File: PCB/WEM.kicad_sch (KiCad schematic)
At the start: 0 parts

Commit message: Started schematic design
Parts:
- added D1: SMF5V0A, Diode_SMD:D_SMF, symbol Diode:SMF5V0A
- added D2: TPD2EUSB30DRTR, TPD2EUSB30DRTR:SOTFL35P100X50-3N, symbol TPD2EUSB30DRTR:TPD2EUSB30DRTR
- added F1: 1206L110THYR, Fuse:Fuse_1206_3216Metric_Pad1.42x1.75mm_HandSolder, symbol 2026-01-18_16-05-31:1206L110THYR
- added J1: USB_C_Receptacle_USB2.0_14P, symbol Connector:USB_C_Receptacle_USB2.0_14P
- added R1, R2: 5.1K, Resistor_SMD:R_0805_2012Metric_Pad1.20x1.40mm_HandSolder, symbol Device:R
- added U1: nRF52840, Package_DFN_QFN:Nordic_AQFN-73-1EP_7x7mm_P0.5mm, symbol MCU_Nordic:nRF52840
- added U2: MCP73871-2CC, Package_DFN_QFN:QFN-20-1EP_4x4mm_P0.5mm_EP2.5x2.5mm, symbol Battery_Management:MCP73871-2CC
- added U3: ~, PAW3395DM-T6QU:DIP-16_PAW3395DM-T6QU, symbol PAW3395DM-T6QU:PAW3395DM-T6QU_C9900026834
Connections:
- new net: J1.A5 (CC1), R1.1
- new net: D1.1 (A1), F1.1
- new net: D1.2 (A2), J1.A4 (VBUS), J1.A9 (VBUS), J1.B4 (VBUS), J1.B9 (VBUS)
- new net: U2.1 (OUT), U2.20 (OUT)
- new net: U2.10 (V_{SS}), U2.11 (V_{SS}), U2.21 (V_{SS})
- new net: U2.14 (V_{BAT}), U2.15 (V_{BAT})
- new net: U2.18 (IN), U2.19 (IN)
- new net: J1.B5 (CC2), R2.1
- new net: U1.A22 (VDD), U1.AD14 (VDD), U1.AD23 (VDD), U1.B1 (VDD), U1.W1 (VDD)
- new net: U1.B7 (VSS), U1.EP (VSS)
- new net GND: D2.3 (GND), J1.A1 (GND), J1.A12 (GND), J1.B1 (GND), J1.B12 (GND), J1.S1 (SHIELD), R1.2, R2.2
- new net USB_D+: D2.1 (D+), J1.A6 (D+), J1.B6 (D+)
- new net USB_D-: D2.2 (D-), J1.A7 (D-), J1.B7 (D-)
- new net VBUS: F1.2
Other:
- note added: "USB-C port"
- title: (none) -> WEM (Wireless Extensible Mouse)

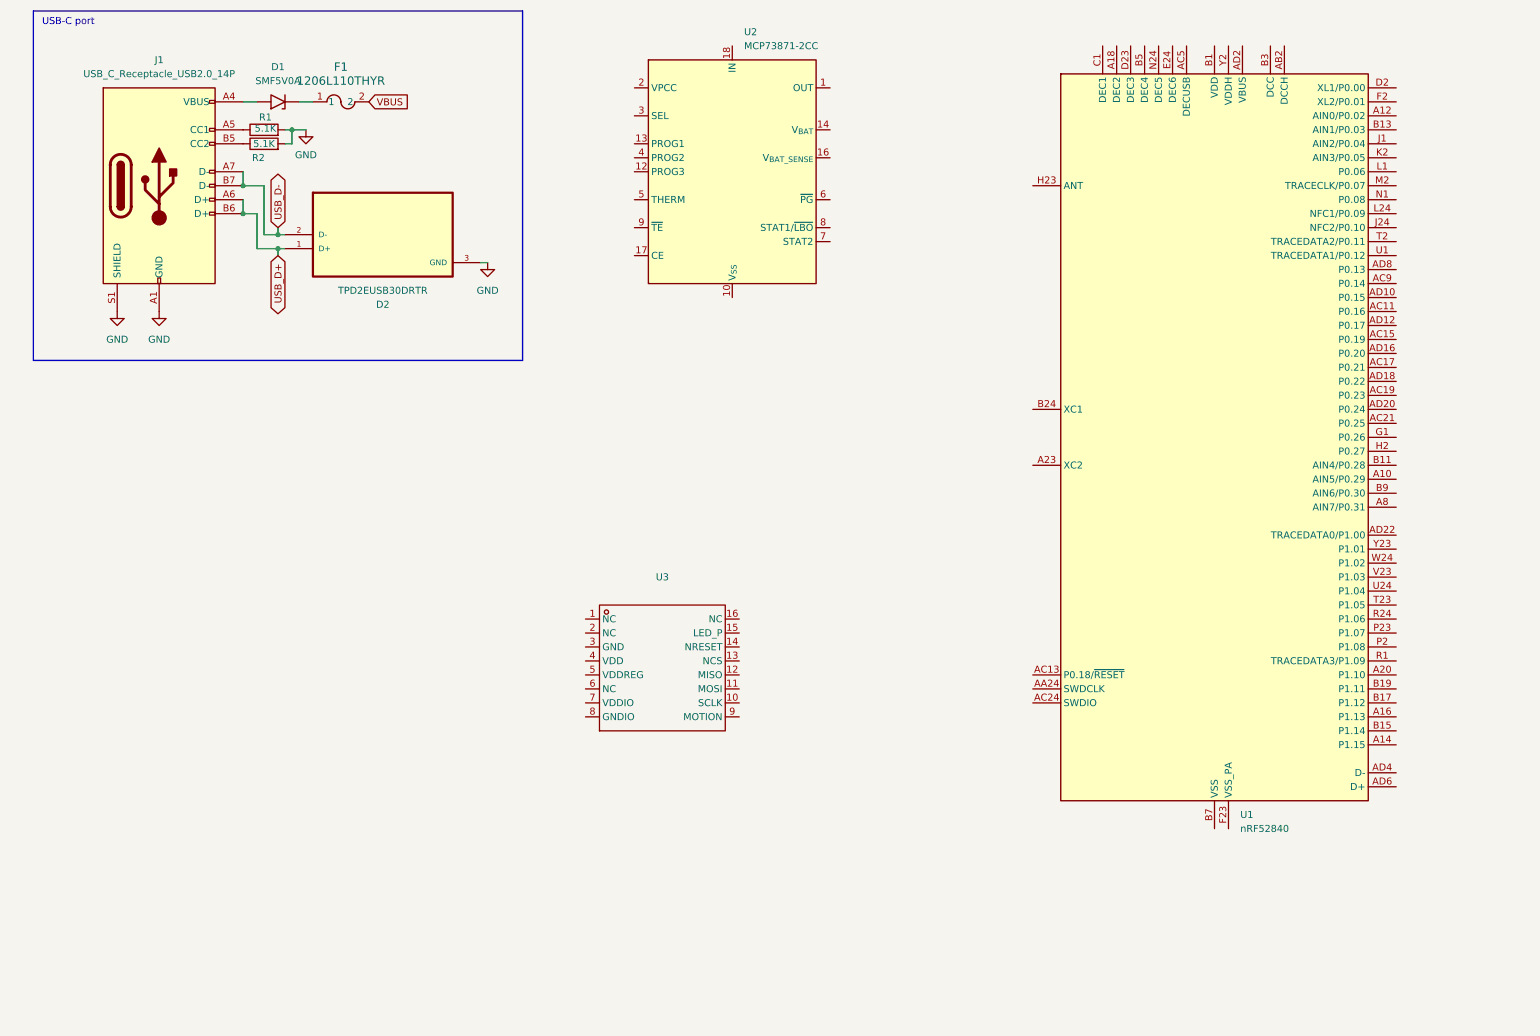
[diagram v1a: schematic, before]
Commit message: Voltage regulators and schematic progress
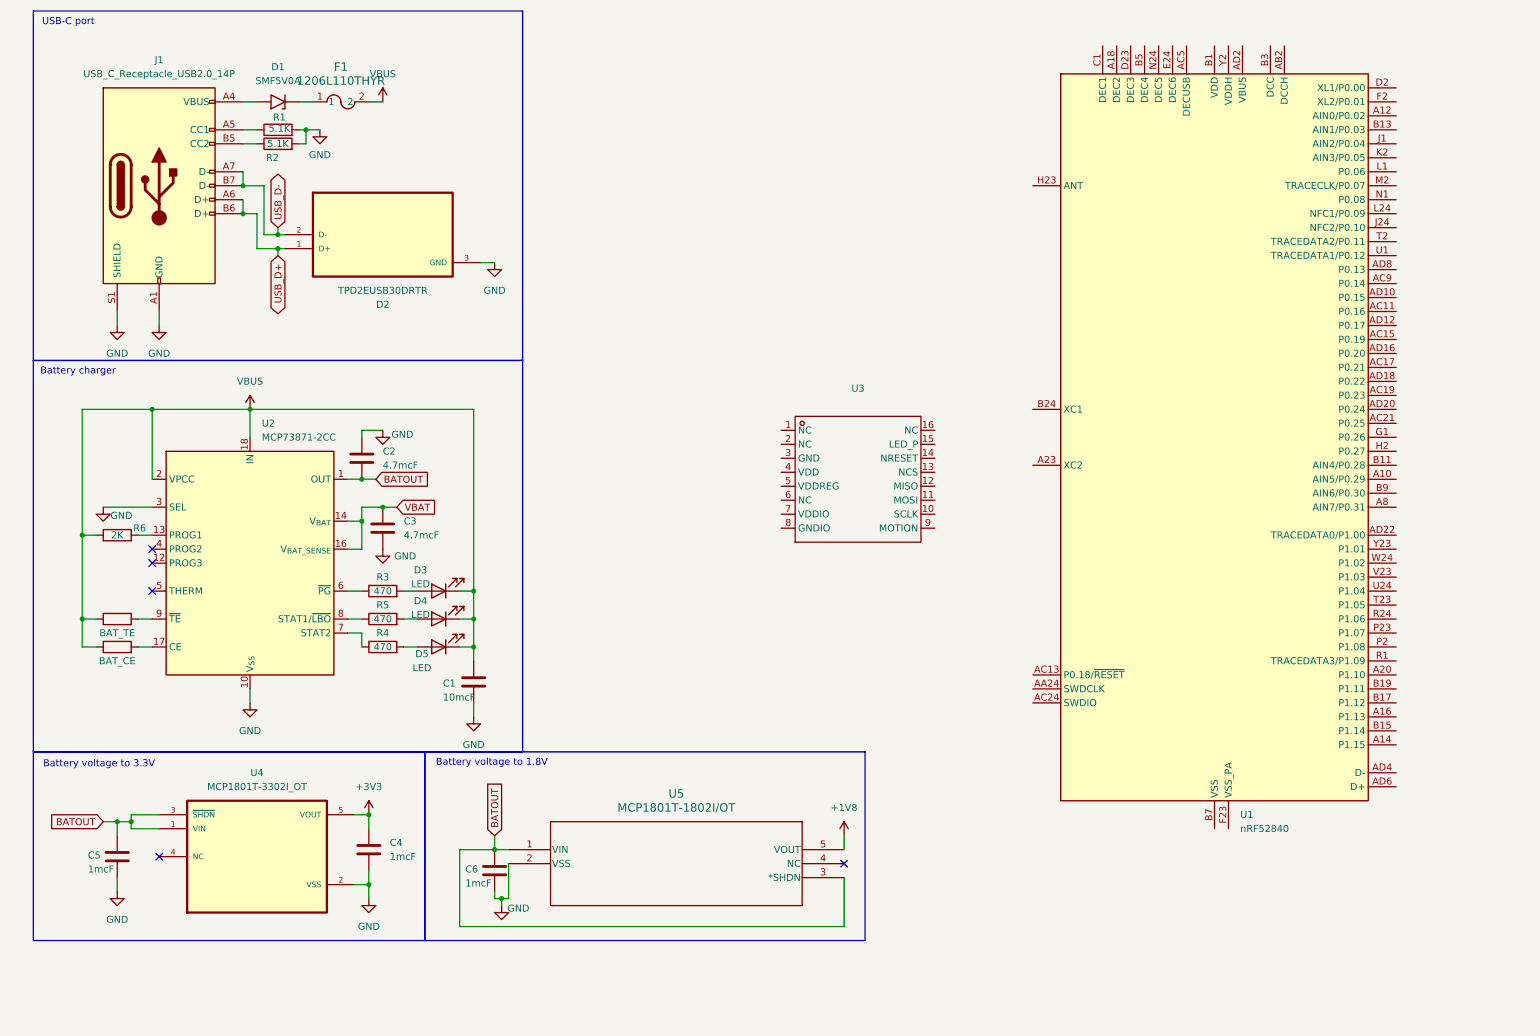
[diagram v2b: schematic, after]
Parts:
- added BAT_CE, BAT_TE: 0, symbol Device:R
- added C1: 10mcF, symbol Device:C
- added C2, C3: 4.7mcF, symbol Device:C
- added C4, C5, C6: 1mcF, symbol Device:C
- added D3, D4, D5: LED, symbol Device:LED
- added R3, R4, R5: 470, symbol Device:R
- added R6: 2K, symbol Device:R
- added U4: MCP1801T-3302I_OT, footprints:SOT-23-5_MC_MCH-M, symbol MCP1801T-3302I_OT:MCP1801T-3302I_OT
- added U5: MCP1801T-1802I/OT, footprints:SOT-23-5_MC_MCH-M, symbol 2026-01-22_18-48-37:MCP1801T-1802I_OT
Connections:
- net GND: now also U2.10 (V_{SS}), U2.11 (V_{SS}), U2.21 (V_{SS}), U2.3 (SEL), C1.2, C2.2, C3.1, C4.2, C5.2, C6.2, U4.2 (VSS), U5.2 (VSS)
- net VBUS: now also U2.18 (IN), U2.19 (IN), U2.2 (VPCC), BAT_CE.1, BAT_TE.1, C1.1, D3.1 (K), D4.1 (K), D5.1 (K), R6.1
- net BATOUT: now reaches U2.1 (OUT), U2.20 (OUT)
- net BATOUT: now also C2.1, C5.1, C6.1, U4.1 (VIN), U4.3 (~{SHDN}), U5.1 (VIN), U5.3 (*SHDN)
- net at U2.13 (PROG1): now also R6.2
- net VBAT: now reaches U2.14 (V_{BAT}), U2.15 (V_{BAT})
- net VBAT: now also U2.16 (V_{BAT_SENSE}), C3.2
- net at U2.17 (CE): now also BAT_CE.2
- net at U2.6 (~{PG}): now also R3.1
- net at U2.7 (STAT2): now also R4.1
- net at U2.8 (STAT1/~{LBO}): now also R5.1
- net at U2.9 (~{TE}): now also BAT_TE.2
- new net: D5.2 (A), R4.2
- new net: D4.2 (A), R5.2
- new net: D3.2 (A), R3.2
- new net +1V8: U5.5 (VOUT)
- new net +3V3: C4.1, U4.5 (VOUT)
- no-connect marks 0 -> 5
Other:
- note added: "Battery charger"
- note added: "Battery voltage to 1.8V"
- note added: "Battery voltage to 3.3V"
- moved on the sheet: R1, R2, U2, U3

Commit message: Mouse wheel encoder amd more work on schematics
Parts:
- added C10: 4.7mcF, symbol Device:C
- added C11, C7, C9: 100nF, symbol Device:C
- added C12, C8: 10mcF, symbol Device:C
- added EXT1, EXT2, EXT3, SWDCLK, SWDIO, SWO: 0, symbol Device:R
- added J2: MCU flashing pins, symbol Connector:Conn_01x05_Socket
- added J3: Extensions' connector, symbol Connector:Conn_01x06_Socket
- added R7: 4.53, symbol Device:R
- added SW1: Kailh Mouse Scroll Wheel Encoder 9mm, wheel_encoder:Kailh Mouse Scroll Wheel Encoder 9mm, symbol Device:RotaryEncoder
- U3: value ~ -> PAW3395DM-T6QU
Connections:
- net +1V8: now also U3.4 (VDD), C7.2, C8.2, R7.2
- net +3V3: now also U3.7 (VDDIO), C11.1, C12.1, J2.1 (Pin_1), J3.1 (Pin_1)
- net GND: now also U3.3 (GND), U3.8 (GNDIO), C10.2, C11.2, C12.2, C7.1, C8.1, C9.2, J2.5 (Pin_5), J3.6 (Pin_6), SW1.C
- net OPTSENSE_RESET: now reaches U3.14 (NRESET)
- net at U3.15 (LED_P): now also R7.1
- net at U3.5 (VDDREG): now also C10.1, C9.1
- net MOTION: now reaches U3.9 (MOTION)
- net SWDCLK: now reaches U1.AA24 (SWDCLK)
- net SWDCLK: now also SWDCLK.2
- net MCU_RESET: now reaches U1.AC13 (P0.18/~{RESET})
- net SWDIO: now reaches U1.AC24 (SWDIO)
- net SWDIO: now also SWDIO.2
- net SWO: now reaches U1.AD22 (TRACEDATA0/P1.00)
- net SWO: now also SWO.1
- net VBAT renamed +BATT
- new net: EXT2.2, J2.3 (Pin_3), SWDCLK.1
- new net: EXT1.2, J2.2 (Pin_2), SWDIO.1
- new net: EXT3.2, J2.4 (Pin_4), SWO.2
- new net RE_A: SW1.A
- new net RE_B: SW1.B
- no-connect marks 5 -> 9
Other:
- note added: "Extensions' and MCU flashing connectors"
- note added: "Mouse wheel encoder"
- note added: "Optical movement sensor"
- moved on the sheet: BAT_CE, BAT_TE, C1, C2, C3, C6, D1, D2, D3, D4, D5, F1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

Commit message: More schematics
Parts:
- removed J3: Extensions' connector, symbol Connector:Conn_01x06_Socket
- added AE1: Antenna, RF_Antenna:Texas_SWRA117D_2.4GHz_Right, symbol Device:Antenna
- added C13: 0.8pF, symbol Device:C
- added C14: 0.5pF, symbol Device:C
- added C15, C19, C23: NC, symbol Device:C
- added C16, C17: 12pF, symbol Device:C
- added C18, C26, C27, C29: 100nF, symbol Device:C
- added C20: 100pF, symbol Device:C
- added C21, C24: 1mcF, symbol Device:C
- added C22, C25, C28: 4.7mcF, symbol Device:C
- added J3: Extensions' connectors, Connector_PinSocket_2.54mm:PinSocket_2x04_P2.54mm_Vertical, symbol Connector_Generic:Conn_02x04_Odd_Even
- added L1: 4.7nH, symbol Device:L
- added SW2, SW3, SW4, SW5, SW6, SW7: D2F, D2F:D2F-F, symbol 2026-01-22_18-51-59:SW1_1COM_2NO_3NC
- added Y1: 32MHz, symbol Device:Crystal
- J2: footprint (none) -> Connector_PinSocket_2.54mm:PinSocket_1x05_P2.54mm_Vertical
- renumbered EXT1 to EXT2.1, EXT2 to EXT2.2, EXT3 to EXT2.3
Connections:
- net +3V3: now also U1.A22 (VDD), U1.AD14 (VDD), U1.AD23 (VDD), U1.B1 (VDD), U1.W1 (VDD), U1.Y2 (VDDH), C24.2, C25.2, C26.2, C27.2, C29.2, J3.1 (Pin_1)
- net GND: now also U1.B7 (VSS), U1.EP (VSS), U1.F23 (VSS_PA), C13.2, C14.2, C15.2, C16.1, C17.1, C18.1, C19.1, C20.1, C21.1, C22.1, C23.1, C24.1, C25.1, C26.1, C27.1, C28.1, C29.1, J3.2 (Pin_2), SW2.1, SW3.1, SW4.1, SW5.1, SW6.1, SW7.1
- net VBUS: now also U1.AD2 (VBUS), C28.2
- net EXT2.2: now reaches EXT2.2.1
- net OPTSENSE_SCLK: now reaches U3.10 (SCLK)
- net OPTSENSE_MOSI: now reaches U3.11 (MOSI)
- net OPTSENSE_MISO: now reaches U3.12 (MISO)
- net OPTSENSE_CS: now reaches U3.13 (NCS)
- net EXT2.1: now reaches EXT2.1.1
- net EXT2.3: now reaches EXT2.3.1
- net at U1.A18 (DEC2): now also C19.2
- net at U1.A23 (XC2): now also C16.2, Y1.1
- net at U1.AC5 (DECUSB): now also C22.2
- net at U1.B24 (XC1): now also C17.2, Y1.2
- net at U1.B5 (DEC4): now also U1.E24 (DEC6), C21.2, C23.2
- net at U1.C1 (DEC1): now also C18.2
- net at U1.D23 (DEC3): now also C20.2
- net at U1.H23 (ANT): now also C13.1, L1.2
- new net: AE1.1 (A), C14.1, C15.1, L1.1
- new net BACK: SW5.2
- new net EXT1.1: J3.3 (Pin_3)
- new net EXT1.2: J3.4 (Pin_4)
- new net EXT1.3: J3.5 (Pin_5)
- new net EXT1.4: J3.6 (Pin_6)
- new net EXT1.5: J3.7 (Pin_7)
- new net EXT1.6: J3.8 (Pin_8)
- new net FORWARD: SW4.2
- new net LMB: SW2.2
- new net MMB: SW6.2
- new net RMB: SW3.2
- new net SMMB: SW7.2
- no-connect marks 9 -> 20
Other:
- note added: "Button switches"
- note added: "nRF52840"
- moved on the sheet: BAT_CE, BAT_TE, C1, C10, C11, C12, C2, C3, C4, C5, C6, C7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

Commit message: Finished schematics
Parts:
- removed SW2, SW3, SW4, SW5, SW6, SW7: D2F, D2F:D2F-F, symbol 2026-01-22_18-51-59:SW1_1COM_2NO_3NC
- removed U5: MCP1801T-1802I/OT, footprints:SOT-23-5_MC_MCH-M, symbol 2026-01-22_18-48-37:MCP1801T-1802I_OT
- added C30: 0.01mcF, Capacitor_SMD:C_0805_2012Metric_Pad1.18x1.45mm_HandSolder, symbol Device:C
- added C31: 10pmcF, Capacitor_SMD:C_0805_2012Metric_Pad1.18x1.45mm_HandSolder, symbol Device:C
- added D6: 1N5817, Diode_THT:D_DO-41_SOD81_P10.16mm_Horizontal, symbol Diode:1N5817
- added J4: Battery, Connector_JST:JST_XH_B2B-XH-A_1x02_P2.50mm_Vertical, symbol Connector:Conn_01x02_Socket
- added J5: Reset, Connector_PinHeader_2.54mm:PinHeader_1x02_P2.54mm_Vertical, symbol Connector:Conn_01x02_Pin
- added R10, R8, R9: 10K, Resistor_SMD:R_0805_2012Metric_Pad1.20x1.40mm_HandSolder, symbol Device:R
- added SW2: LMB, Kailh:Kailh MI627301D07, symbol Switch:SW_Push
- added SW3: MMB, Kailh:Kailh MI627301D07, symbol Switch:SW_Push
- added SW4: RMB, Kailh:Kailh MI627301D07, symbol Switch:SW_Push
- added SW5: FORWARD, Kailh:Kailh MI627301D07, symbol Switch:SW_Push
- added SW6: BACK, Kailh:Kailh MI627301D07, symbol Switch:SW_Push
- added SW7: SMMB, Kailh:Kailh MI627301D07, symbol Switch:SW_Push
- added SW9: Power/mode switch, SW-TH_SSSS223600:SW-TH_SSSS223600, symbol Switch:SW_DP3T
- added U5: LT1761ES5-2-TRMPBF, footprints:S_5_ADI, symbol 2026-01-25_10-34-58:LT1761ES5-2-TRMPBF
- BAT_CE1: renamed from BAT_CE; footprint (none) -> Resistor_SMD:R_0805_2012Metric_Pad1.20x1.40mm_HandSolder
- BAT_TE1: renamed from BAT_TE; footprint (none) -> Resistor_SMD:R_0805_2012Metric_Pad1.20x1.40mm_HandSolder
- C1, C10, C11, C12, C13, C14, C15, C16, C17, C18, C19, C2, C20, C21, C22, C23, C24, C25, C26, C27, C28, C29, C3, C4, C5, C6, C7, C8, C9: footprint (none) -> Capacitor_SMD:C_0805_2012Metric_Pad1.18x1.45mm_HandSolder
- D3, D4, D5: footprint (none) -> LED_SMD:LED_0805_2012Metric_Pad1.15x1.40mm_HandSolder
- EXT2.1, EXT2.2, EXT2.3, R6: footprint (none) -> Resistor_SMD:R_0805_2012Metric_Pad1.20x1.40mm_HandSolder
- J1: footprint (none) -> Connector_USB:USB_C_Receptacle_GCT_USB4085
- L1: footprint (none) -> Inductor_SMD:L_0402_1005Metric_Pad0.77x0.64mm_HandSolder
- R3, R4: value 470 -> 440; footprint (none) -> Resistor_SMD:R_0805_2012Metric_Pad1.20x1.40mm_HandSolder
- R5: value 470 -> 620; footprint (none) -> Resistor_SMD:R_0805_2012Metric_Pad1.20x1.40mm_HandSolder
- R7: value 4.53 -> 6.8; footprint (none) -> Resistor_SMD:R_0805_2012Metric_Pad1.20x1.40mm_HandSolder
- SW1: footprint wheel_encoder:Kailh Mouse Scroll Wheel Encoder 9mm -> Kailh:Kailh Mouse Scroll Wheel Encoder 9mm
- SWDCLK1: renamed from SWDCLK; footprint (none) -> Resistor_SMD:R_0805_2012Metric_Pad1.20x1.40mm_HandSolder
- SWDIO1: renamed from SWDIO; footprint (none) -> Resistor_SMD:R_0805_2012Metric_Pad1.20x1.40mm_HandSolder
- SWO1: renamed from SWO; footprint (none) -> Resistor_SMD:R_0805_2012Metric_Pad1.20x1.40mm_HandSolder
- X1: renamed from Y1; footprint (none) -> Crystal:Crystal_SMD_2016-4Pin_2.0x1.6mm
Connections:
- net +3V3: now also R10.2, R8.2, R9.2
- net +BATT: now also J4.1 (Pin_1)
- net BACK: now also U1.AC9 (P0.14), SW6.2
- net BATOUT: now also SW9.3; no longer C5.1, C6.1, U4.1 (VIN), U4.3 (~{SHDN})
- net EXT1.1: now also U1.Y23 (P1.01)
- net EXT1.2: now also U1.W24 (P1.02)
- net EXT1.3: now also U1.V23 (P1.03)
- net EXT1.4: now also U1.U24 (P1.04)
- net EXT1.5: now also U1.T23 (P1.05)
- net EXT1.6: now also U1.R24 (P1.06)
- net EXT2.1: now also U1.B11 (AIN4/P0.28)
- net EXT2.2: now also U1.A10 (AIN5/P0.29)
- net EXT2.3: now also U1.B9 (AIN6/P0.30)
- net FORWARD: now also U1.AD8 (P0.13), SW5.2
- net GND: now also C31.2, J4.2 (Pin_2), J5.2 (Pin_2), SW2.1, SW3.1, SW4.1, SW5.1, SW6.1, SW7.1, SW9.7, U5.2 (GND)
- net LMB: now also U1.AD10 (P0.15), SW2.2
- net MMB: now also U1.AC11 (P0.16), SW3.2
- net MOTION: now also U1.AD16 (P0.20), R10.1
- net OPTSENSE_CS: now also U1.AC15 (P0.19)
- net OPTSENSE_MISO: now also U1.AC17 (P0.21), R8.1
- net OPTSENSE_MOSI: now also U1.AD18 (P0.22)
- net OPTSENSE_SCLK: now also U1.AC19 (P0.23)
- net RE_A: now also U1.G1 (P0.26)
- net RE_B: now also U1.H2 (P0.27)
- net RMB: now also U1.AD12 (P0.17), SW4.2
- net SMMB: now also U1.U1 (TRACEDATA1/P0.12), SW7.2
- net USB_D+: now also U1.AD6 (D+)
- net USB_D-: now also U1.AD4 (D-)
- net VBUS: now also D3.2 (A), D4.2 (A), D5.2 (A), D6.2 (A); no longer D3.1 (K), D4.1 (K), D5.1 (K)
- net at R4.2: now also D5.1 (K); no longer D5.2 (A)
- net at R5.2: now also D4.1 (K); no longer D4.2 (A)
- net at R3.2: now also D3.1 (K); no longer D3.2 (A)
- net BLE_MODE: now reaches U1.P2 (P1.08)
- net BLE_MODE: now also SW9.8
- net DONGLE_MODE: now reaches U1.P23 (P1.07)
- net DONGLE_MODE: now also SW9.6
- net +1V8 renamed +2V
- net +2V: now also C30.1, C31.1, U5.5 (OUT)
- net MCU_RESET: no longer names the net of U1.AC13 (P0.18/~{RESET})
- net MCU_RESET: now also J5.1 (Pin_1)
- net OPTSENSE_RESET: no longer names the net of U3.14 (NRESET)
- net OPTSENSE_RESET: now also R9.1
- new net: C30.2, U5.4 (BYP)
- new net POWER: C5.1, C6.1, D6.1 (K), SW9.2, SW9.4, U4.1 (VIN), U4.3 (~{SHDN}), U5.1 (IN), U5.3 (*SHDN)
- no-connect marks 20 -> 35
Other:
- note added: "Battery connector"
- note added: "Battery voltage to 2V"
- note added: "Power/mode switch"
- note removed: "Battery voltage to 1.8V"
- moved on the sheet: C2, C3, D3, D4, D5, EXT2.1, EXT2.2, EXT2.3, J2, J3, SWDCLK1, SWDIO1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

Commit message: Schematics modifications and firmware
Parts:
- removed R10, R9: 10K, Resistor_SMD:R_0805_2012Metric_Pad1.20x1.40mm_HandSolder, symbol Device:R
- removed SW9: Power/mode switch, SW-TH_SSSS223600:SW-TH_SSSS223600, symbol Switch:SW_DP3T
- added C32: 10nF, Capacitor_SMD:C_0805_2012Metric_Pad1.18x1.45mm_HandSolder, symbol Device:C
- added J6: Battery jumper, Connector_PinHeader_2.54mm:PinHeader_1x02_P2.54mm_Vertical, symbol Connector:Conn_01x02_Pin
- added R11: 4M, Resistor_SMD:R_0805_2012Metric_Pad1.20x1.40mm_HandSolder, symbol Device:R
- added R12: 10M, Resistor_SMD:R_0805_2012Metric_Pad1.20x1.40mm_HandSolder, symbol Device:R
- added SW8: ON/OFF, Kailh:Kailh MI627301D07, symbol Switch:SW_Push
- D6: footprint Diode_THT:D_DO-41_SOD81_P10.16mm_Horizontal -> Diode_SMD:D_SOD-323F
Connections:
- net +BATT: now also R11.1
- net BATOUT: now also J6.1 (Pin_1)
- net GND: now also C32.2, R12.2, SW8.1
- net POWER: now also J6.2 (Pin_2)
- net OPTSENSE_RESET: now reaches U3.14 (NRESET)
- net OPTSENSE_RESET: now also U1.AD20 (P0.24)
- net at U1.A12 (AIN0/P0.02): now also C32.1, R11.2, R12.1
- net BLE_MODE: no longer names the net of U1.P2 (P1.08)
- net DONGLE_MODE renamed POWER_SWITCH
- net POWER_SWITCH: now also SW8.2
- no-connect marks 35 -> 31
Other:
- note added: "Battery jumper"
- note added: "Power switch"
- note removed: "Power/mode switch"
